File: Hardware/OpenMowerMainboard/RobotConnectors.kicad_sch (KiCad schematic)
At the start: 27 parts, among them IC1 74ALVC164245DGG,11, J1 Conn_02x11_Top_Bottom, J10 Conn_01x05, J11 Conn_01x03_Male, J12 Conn_01x03_Male, J13 Conn_01x03_Male, J14 Conn_01x03_Male, J17 Conn_01x02, J18 Conn_01x02, J19 Conn_01x04, J2 Conn_02x04_Top_Bottom, J3 Conn_01x02, J4 Conn_01x05, J5 Conn_01x04, J6 Conn_01x04, J7 Conn_01x04, J8 Conn_01x04, J9 Conn_01x04

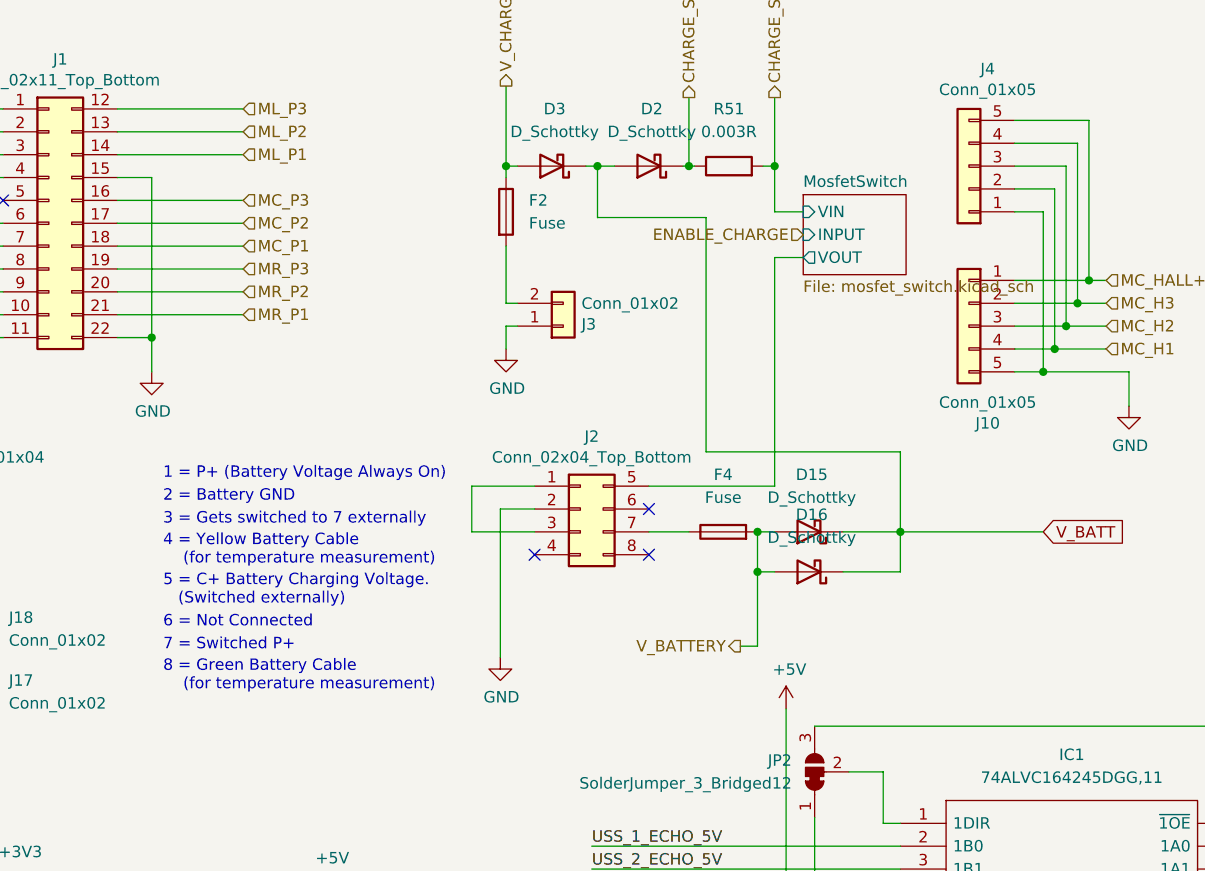
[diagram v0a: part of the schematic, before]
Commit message: mainboard: landroid battery connector
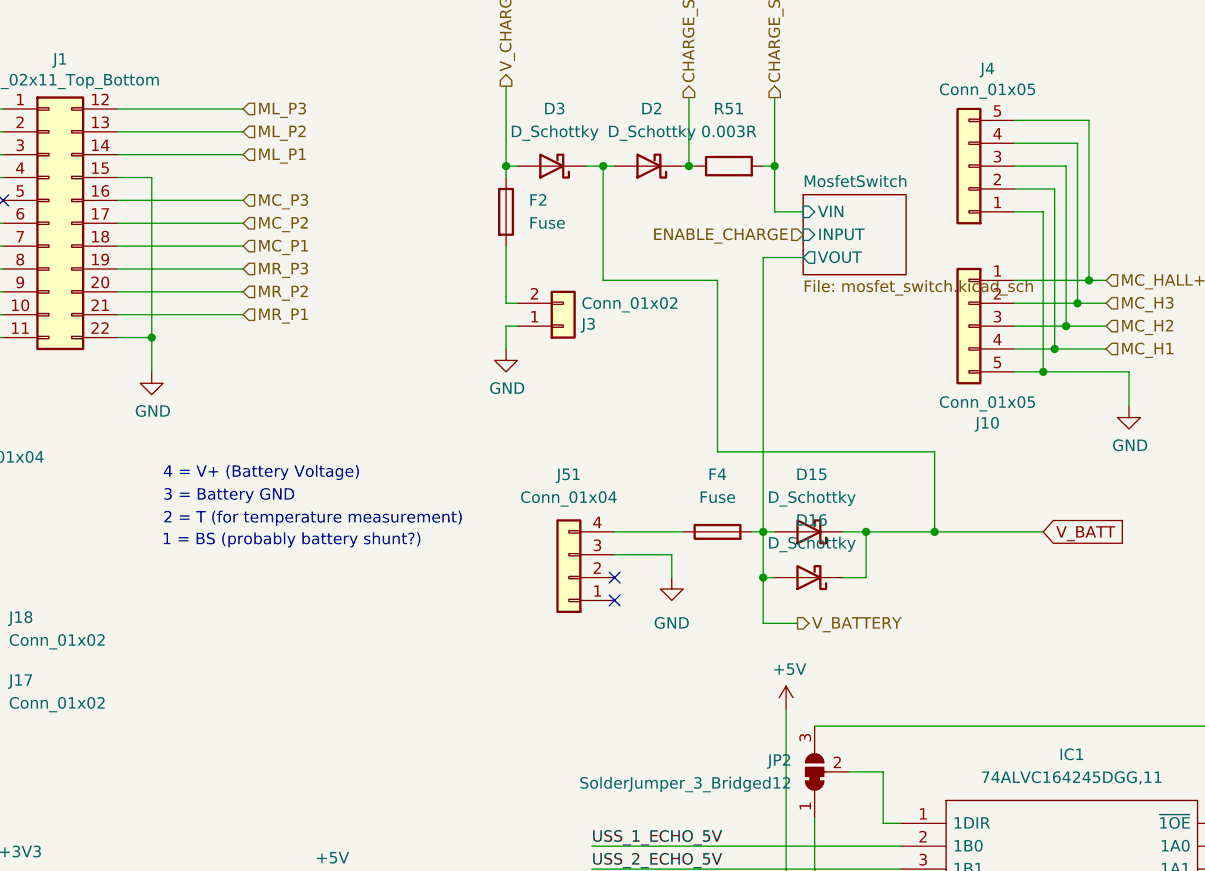
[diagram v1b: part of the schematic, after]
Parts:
- removed J2: Conn_02x04_Top_Bottom, Connector_Molex:Molex_Mini-Fit_Jr_5566-08A_2x04_P4.20mm_Vertical, symbol Connector_Generic:Conn_02x04_Top_Bottom
- added J51: Conn_01x04, Connector_Molex:Molex_Mini-Fit_Jr_5566-04A_2x02_P4.20mm_Vertical, symbol Connector_Generic:Conn_01x04
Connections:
- net GND: now also J51.3 (Pin_3)
- net at F4.1: now also J51.4 (Pin_4)
- no-connect marks 10 -> 9
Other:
- note added: "1 = BS (probably battery shunt?)"
- note added: "2 = T (for temperature measurement)"
- note added: "3 = Battery GND"
- note added: "4 = V+ (Battery Voltage)"
- note removed: "1 = P+ (Battery Voltage Always On)"
- note removed: "2 = Battery GND"
- note removed: "3 = Gets switched to 7 externally"
- note removed: "4 = Yellow Battery Cable (for temperature measurement)"
- note removed: "5 = C+ Battery Charging Voltage. (Switched externally)"
- note removed: "6 = Not Connected"
- note removed: "7 = Switched P+"
- note removed: "8 = Green Battery Cable (for temperature measurement)"
- moved on the sheet: D16, F4
